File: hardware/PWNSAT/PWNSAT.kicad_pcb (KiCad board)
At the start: 2 copper layers, 83 x 83 mm, 117 parts, among them J2 Conn_01x04_Pin, J3 Sensors, J4 USB_A, J5 USB_A, J6 Source, SW1 SW_Push, SW2 SW_Push, SW4 USB Selector, U2 W25N02KVZEIR, U3 EA3059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

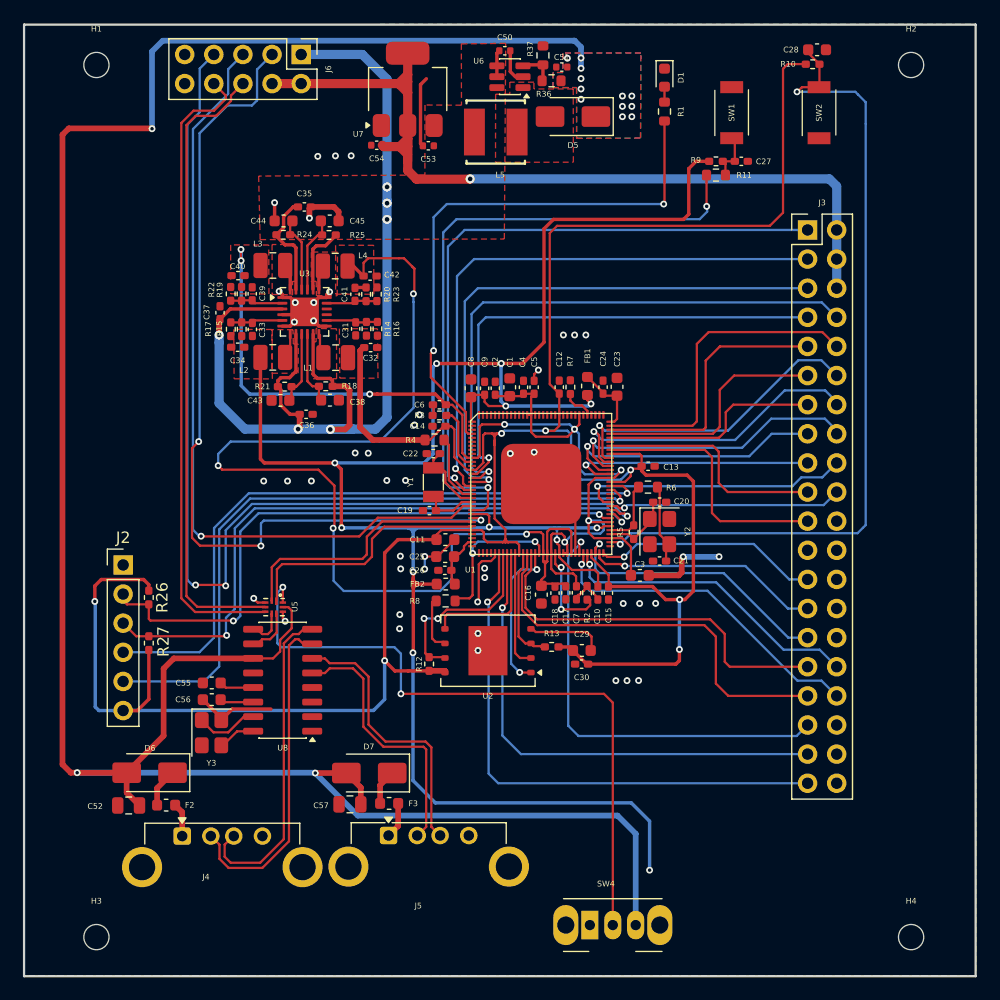
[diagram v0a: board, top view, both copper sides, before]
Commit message: fix(Hw):Tracks_modified
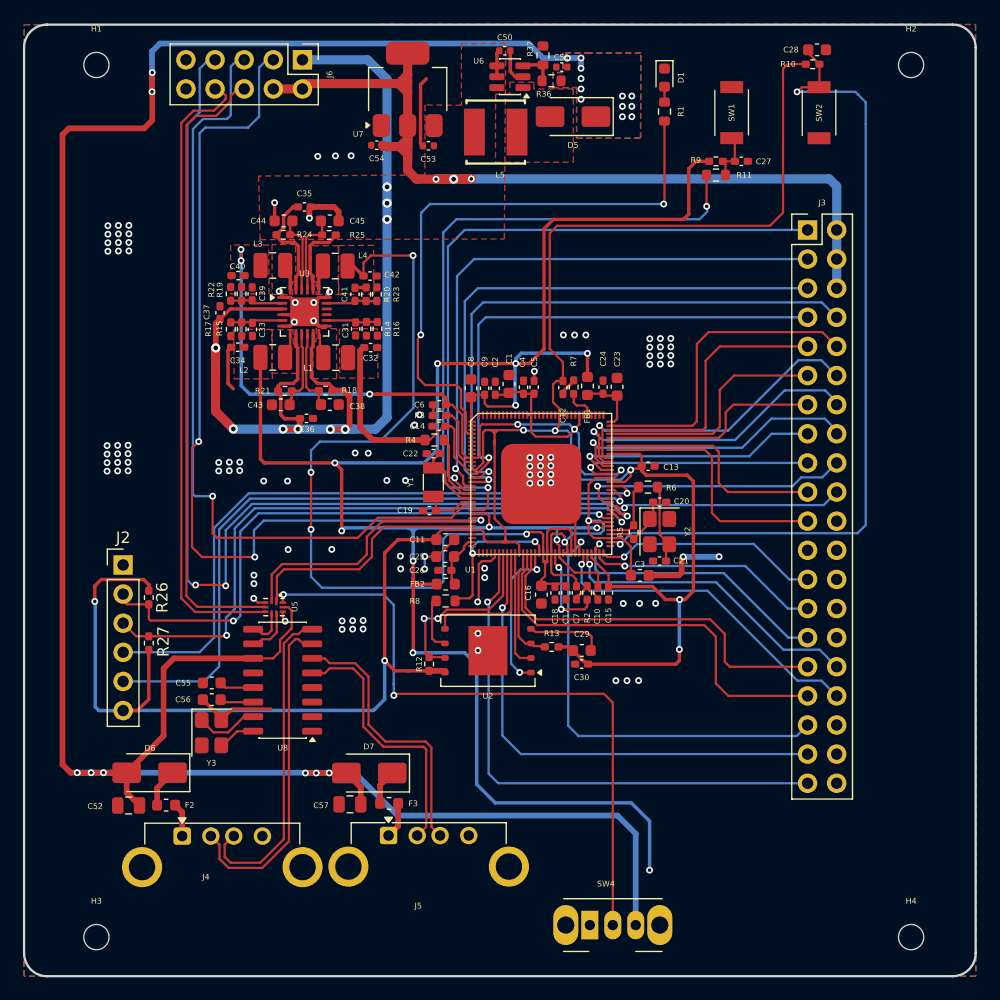
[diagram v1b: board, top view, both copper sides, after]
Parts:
- moved J6 0.48 mm to (44.2, 21.2)
- moved C43 0.38 mm to (42.3, 51.3)
- moved C38 0.38 mm to (46.6, 51.3)
- moved R21 0.37 mm to (42.7, 50.1)
- moved R18 0.37 mm to (46.2, 50.0)
- moved C36 0.36 mm to (44.6, 52.5)
- moved C12 0.32 mm to (67.0, 49.8), turned to -90 degrees
- moved C1 0.30 mm to (62.2, 49.5)
- moved R7 0.29 mm to (67.9, 49.8)
- turned FB1 to -90 degrees
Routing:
- net /core/VCC_DDR: track 97.9 -> 82.8 mm
- net +3.3V: track 78.7 -> 86.5 mm, vias 1 -> 3
- net GND: track 88.1 -> 93.1 mm, vias 47 -> 106
- net /core/LED: track 48.5 -> 51.9 mm
- net VCC: track 110.2 -> 113.5 mm, vias 6 -> 9
- net +5V: track 209.8 -> 212.6 mm, vias 15 -> 20
- net /Source_Connector/USB_DET: track 74.7 -> 77.2 mm
- net /Sensor/R1_BUSY: track 24.1 -> 22.2 mm
- net /USB_Selector/S: track 59.3 -> 57.5 mm
- net +1V8: track 182.4 -> 183.9 mm
- net /Source_Connector/Battery: track 68.9 -> 70.3 mm
- net /Sensor/R1_RST: track 21.9 -> 21.1 mm
- net +3V3: track 239.6 -> 240.3 mm
- net /power_supply/EN1: track 6.59 -> 7.20 mm
- net /core/SZQ: track 8.68 -> 8.08 mm
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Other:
- outline, holes or cut-outs redrawn

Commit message: feat(Hw):Labels_Added
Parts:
- added G***: LOGO, Aesthetics:electronic_cats_logo_8x6, F.Cu at (29.3, 38.5)
- added G***: LOGO, Aesthetics:electronic_cats_logo_8x6, B.Cu at (82.9, 39.8)
- added REF**: OSHW-Logo_5.7x6mm_SilkScreen, Symbol:OSHW-Logo_5.7x6mm_SilkScreen, B.Cu at (35.8, 40.0)
- added kibuzzard-6985157B: G***, kibuzzard-6985157B, B.Cu at (60.3, 31.9)
- added kibuzzard-6985158A: G***, kibuzzard-6985158A, F.Cu at (29.4, 33.4)
- added kibuzzard-6985158A: G***, kibuzzard-6985158A, B.Cu at (60.3, 49.2)
- added kibuzzard-6985168F: G***, kibuzzard-6985168F, F.Cu at (67.8, 91.8)
- added kibuzzard-698516AC: G***, kibuzzard-698516AC, F.Cu at (74.9, 91.6)
- added kibuzzard-698516D4: G***, kibuzzard-698516D4, F.Cu at (38.9, 28.3)
- added kibuzzard-698516F5: G***, kibuzzard-698516F5, F.Cu at (82.1, 60.1)
- added kibuzzard-698517BF: G***, kibuzzard-698517BF, F.Cu at (24.4, 67.9)
- added kibuzzard-698517CD: G***, kibuzzard-698517CD, F.Cu at (24.4, 70.4)
- added kibuzzard-698517E4: G***, kibuzzard-698517E4, F.Cu at (24.0, 72.9)
- added kibuzzard-698517F0: G***, kibuzzard-698517F0, F.Cu at (24.0, 75.3)
- added kibuzzard-69851805: G***, kibuzzard-69851805, F.Cu at (24.4, 78.0)
- added kibuzzard-69851812: G***, kibuzzard-69851812, F.Cu at (24.4, 65.3)

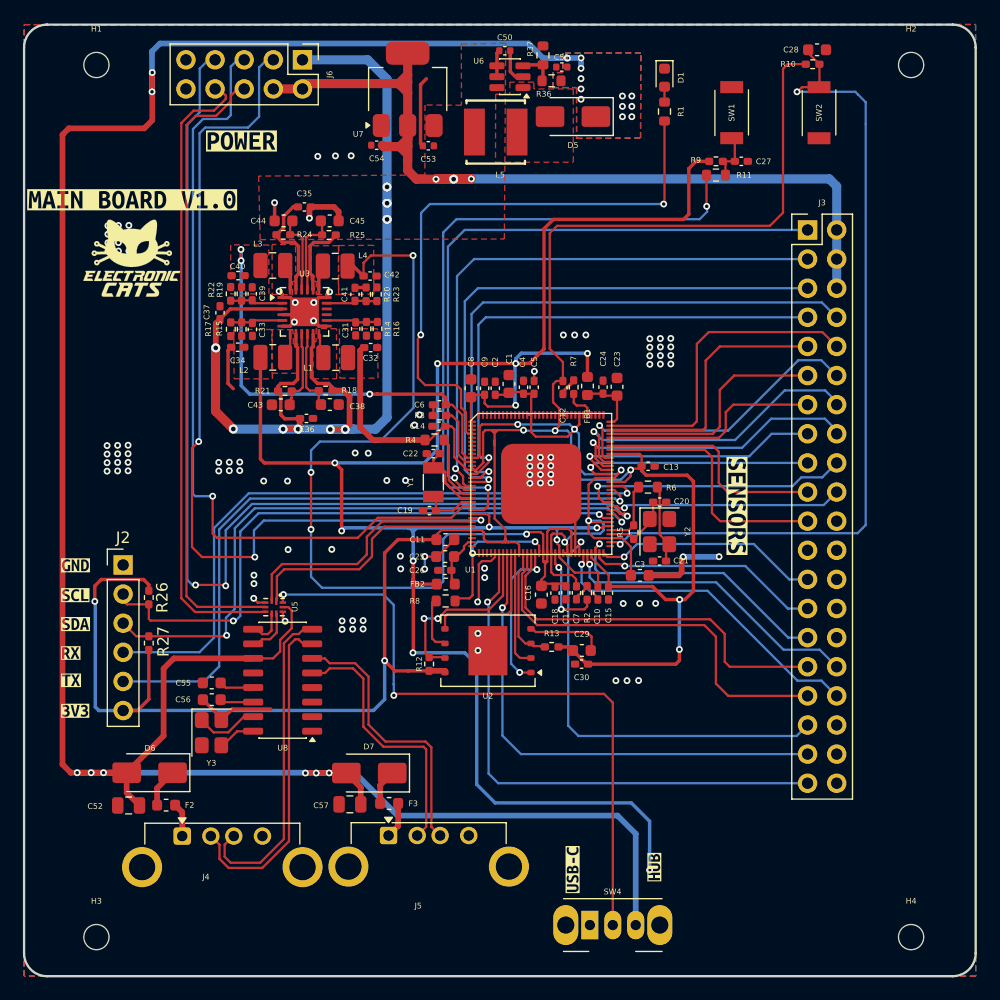
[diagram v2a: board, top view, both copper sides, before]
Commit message: feat(Hw):Update_Labels
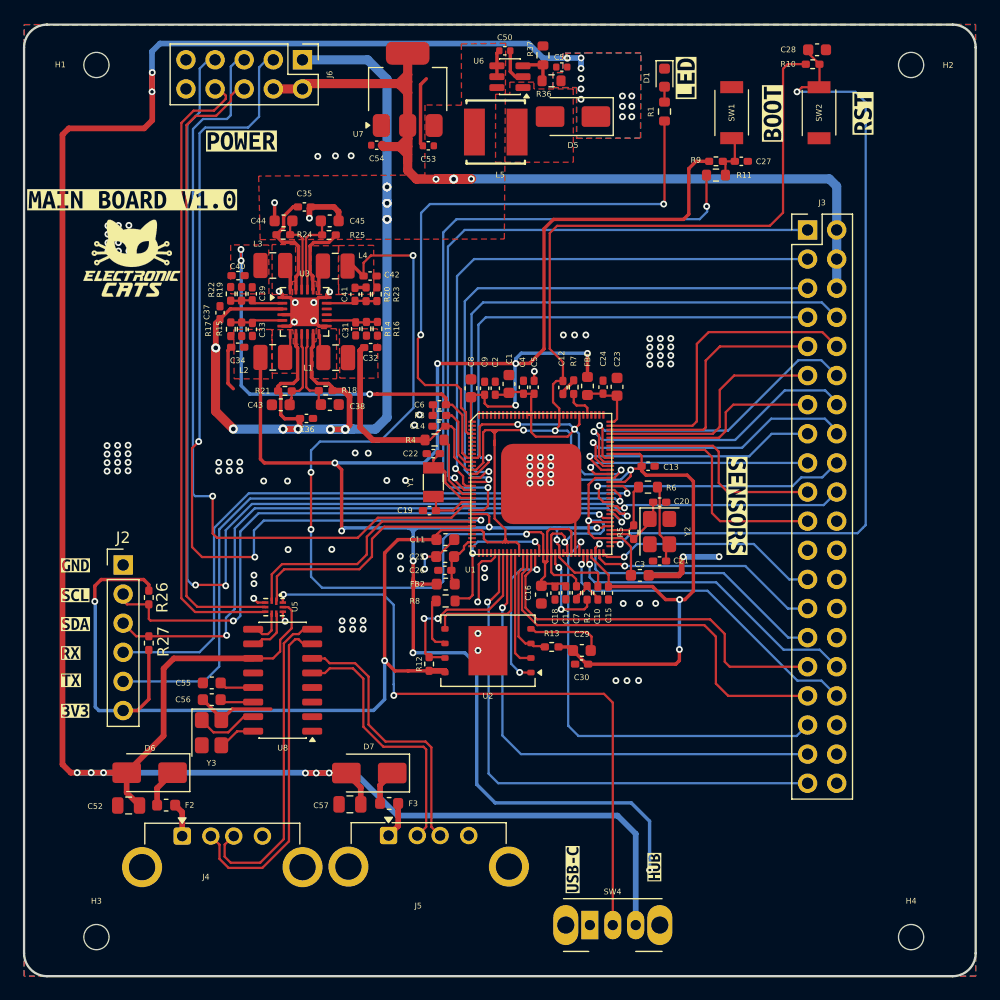
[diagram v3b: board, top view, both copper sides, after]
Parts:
- added kibuzzard-698615E5: G***, kibuzzard-698615E5, F.Cu at (93.1, 25.9)
- added kibuzzard-69861606: G***, kibuzzard-69861606, F.Cu at (85.2, 25.9)
- added kibuzzard-6986164F: G***, kibuzzard-6986164F, F.Cu at (77.7, 22.8)

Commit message: feat(Hw):labels_updated
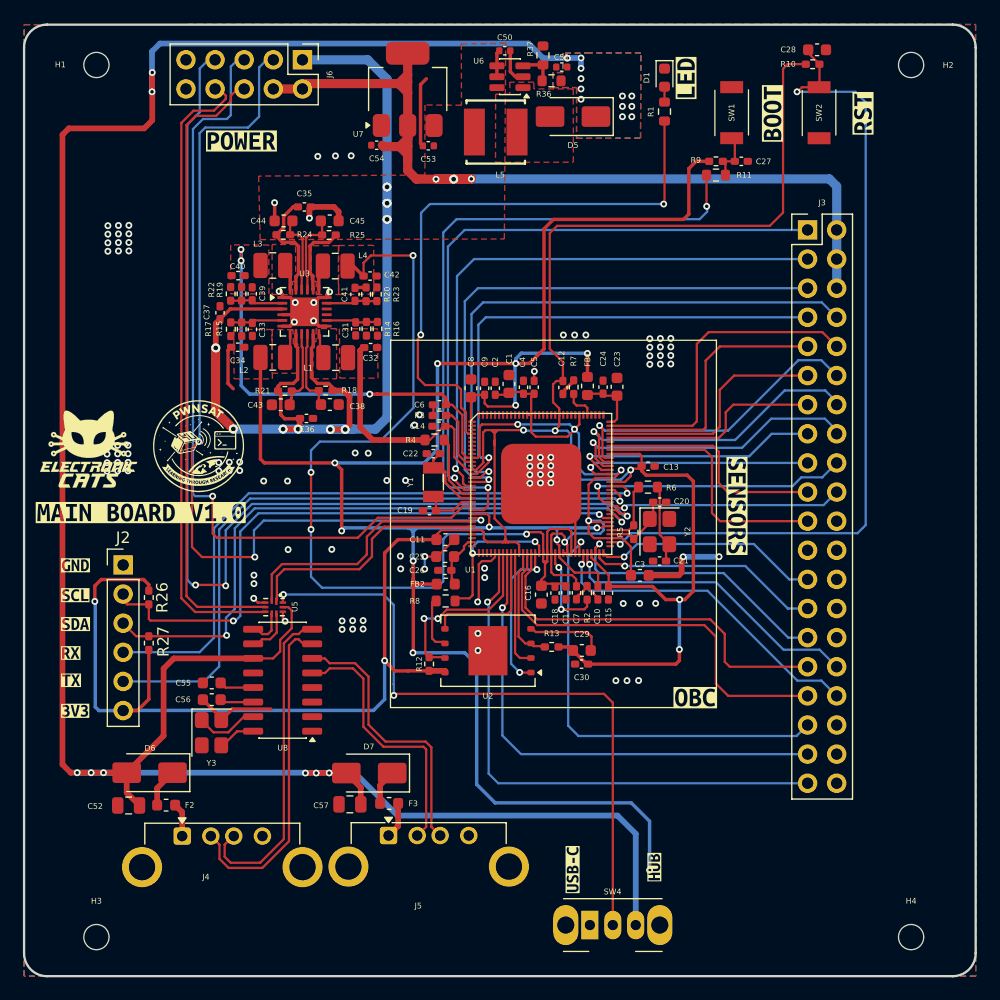
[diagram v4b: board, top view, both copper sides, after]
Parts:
- added kibuzzard-69866D69: G***, kibuzzard-69866D69, F.Cu at (78.5, 76.8)
- moved kibuzzard-6985158A 27.3 mm to (30.1, 60.7)
- moved G*** 17.1 mm to (25.6, 55.2)

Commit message: fix(Hw):Label_Main_Updated
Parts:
- removed kibuzzard-69866D69: G***, kibuzzard-69866D69
- added kibuzzard-6989FAE0: G***, kibuzzard-6989FAE0, F.Cu at (75.4, 75.0)
- added kibuzzard-6989FAEE: G***, kibuzzard-6989FAEE, F.Cu at (75.4, 76.8)

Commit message: feat(Hw):BoM´s_Updated
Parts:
- C32, C34, C40, C42: value 22uf -> 22uF; footprint Capacitor_SMD:C_0402_1005Metric_Pad0.74x0.62mm_HandSolder -> Capacitor_SMD:C_0402_1005Metric
